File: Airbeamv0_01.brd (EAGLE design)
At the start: 91.4 x 74.3 mm, 92 parts

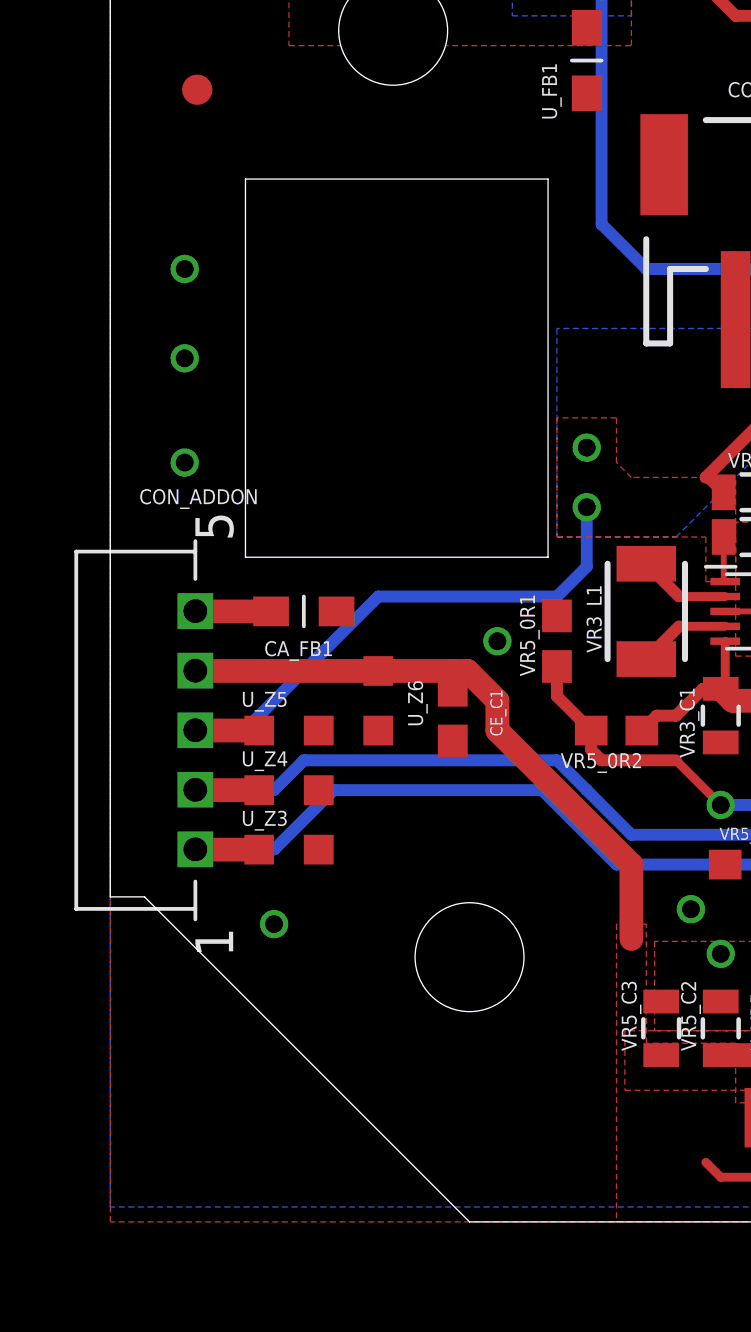
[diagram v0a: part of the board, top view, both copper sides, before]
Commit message: changed to Chris's new cutout
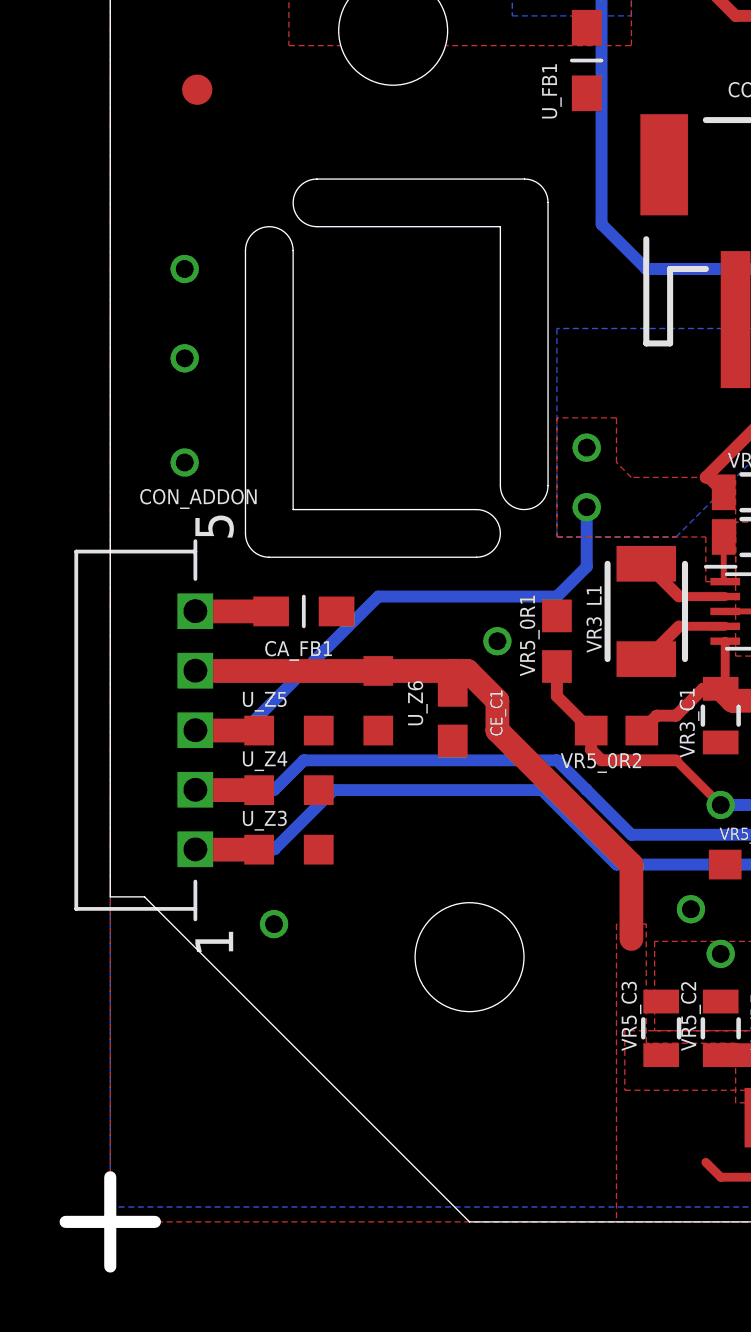
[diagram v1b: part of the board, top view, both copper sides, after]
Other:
- board size 91.4 x 74.3 mm -> 92.9 x 75.8 mm

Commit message: Final version! We are ordering this one!
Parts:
- VR_FUSE: value PTCSMD-W -> 1A
- moved U_C2 1.87 mm to (23.8, 49.2), turned to 270 degrees
- moved U_C1 1.35 mm to (21.3, 49.2), turned to 270 degrees
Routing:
- net VUSB: track 106.9 -> 102.5 mm
- net V_BAT: track 47.1 -> 49.4 mm
- net N$13: track 23.2 -> 24.6 mm

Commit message: Final version! We are ordering this one! 1
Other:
- board size 92.9 x 75.8 mm -> 91.4 x 74.3 mm
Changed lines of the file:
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@@
 <vertex x="77.5" y="33"/>
 </polygon>
-<wire x1="0" y1="1.5" x2="0" y2="-1.5" width="0.4064" layer="20"/>
-<wire x1="-1.5" y1="0" x2="1.5" y2="0" width="0.4064" layer="20"/>
 <wire x1="14.70025" y1="24.72055" x2="14.70025" y2="34.23285" width="0.025" layer="20"/>
 <wire x1="5.32765" y1="22.32025" x2="12.29995" y2="22.32025" width="0.025" layer="20"/>

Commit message: Ordering this board (not the other one)
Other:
- board size 91.4 x 74.3 mm -> 92.9 x 75.3 mm

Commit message: Ordering this board (not the other one)
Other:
- board size 92.9 x 75.3 mm -> 91.4 x 74.3 mm
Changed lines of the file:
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@@
 <wire x1="14.70025" y1="34.23285" x2="13.91285" y2="35.02025" width="0.025" layer="49" curve="90"/>
 <wire x1="4.54025" y1="23.10765" x2="5.32765" y2="22.32025" width="0.025" layer="49" curve="90"/>
-<wire x1="0" y1="1" x2="0" y2="-1" width="0.4064" layer="20"/>
-<wire x1="-1.5" y1="0" x2="1.5" y2="0" width="0.4064" layer="20"/>
 <circle x="13.90015" y="23.12035" radius="0.79375" width="0.025" layer="49"/>
 <circle x="13.90015" y="34.22015" radius="0.79375" width="0.025" layer="49"/>
